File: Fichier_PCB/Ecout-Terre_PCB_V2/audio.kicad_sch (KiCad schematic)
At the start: 32 parts, among them J12 Conn_test_ampli, J14 AudioJack_Mono, U5 TL072, U6 LM386

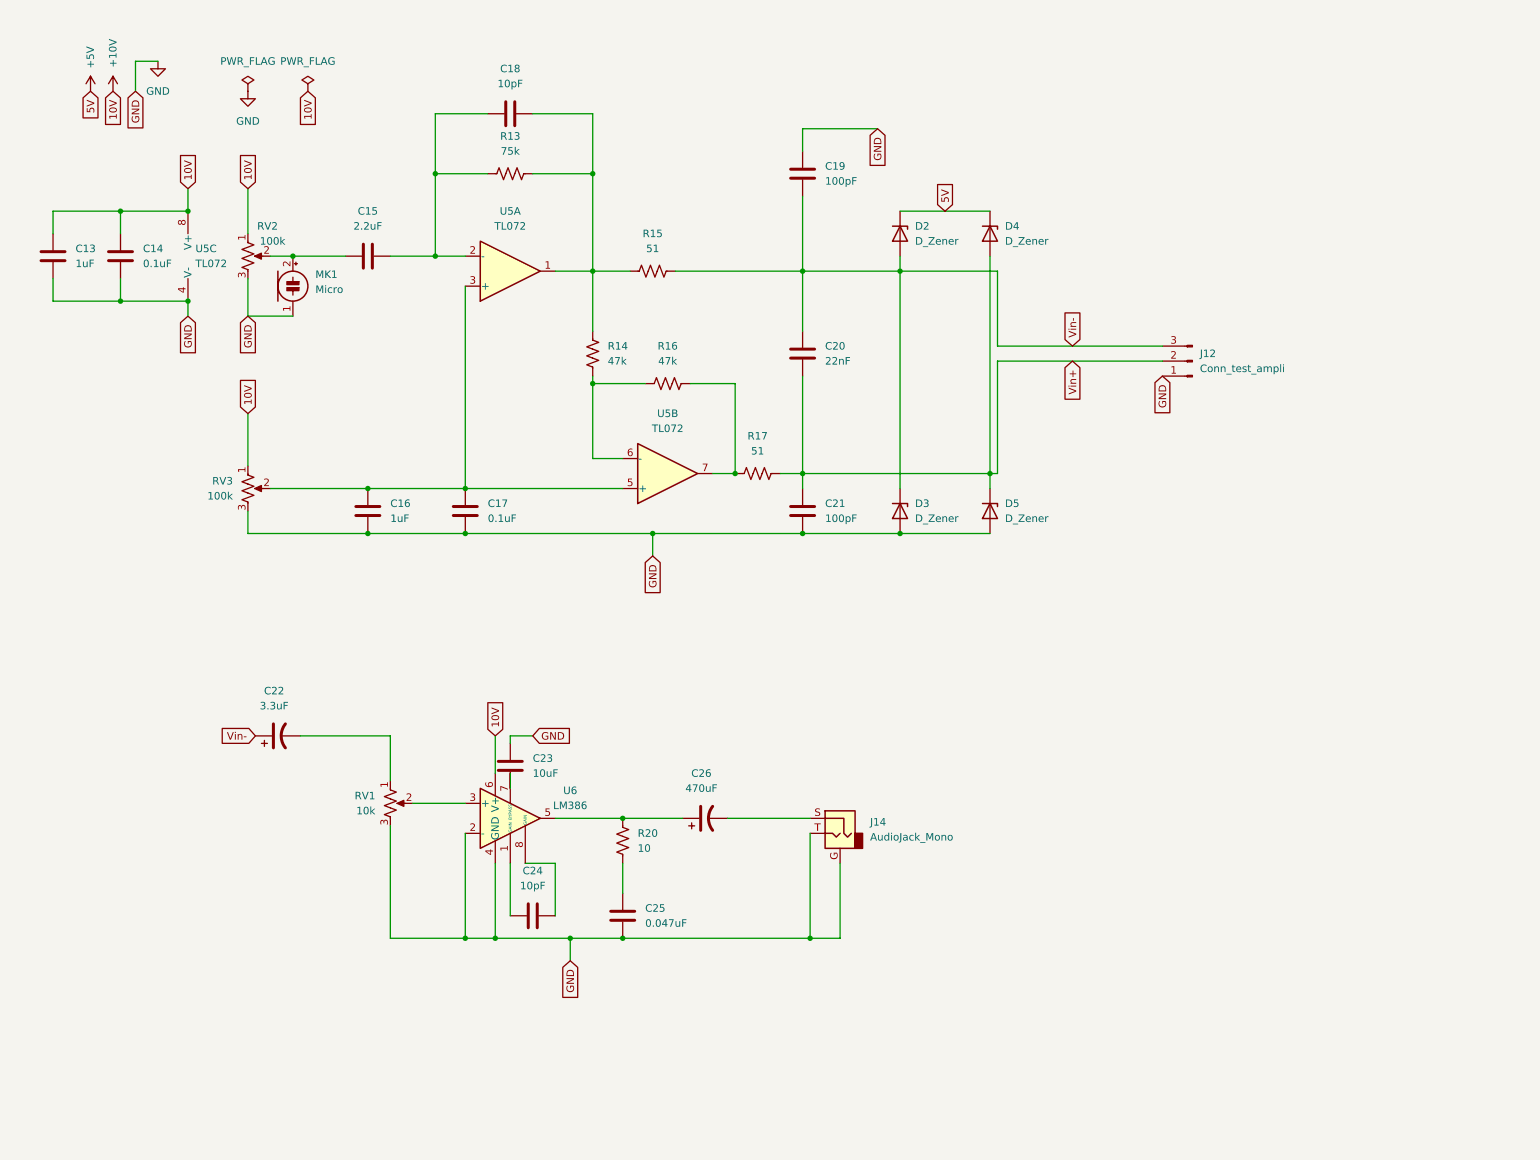
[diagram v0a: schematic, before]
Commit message: Trace pcb
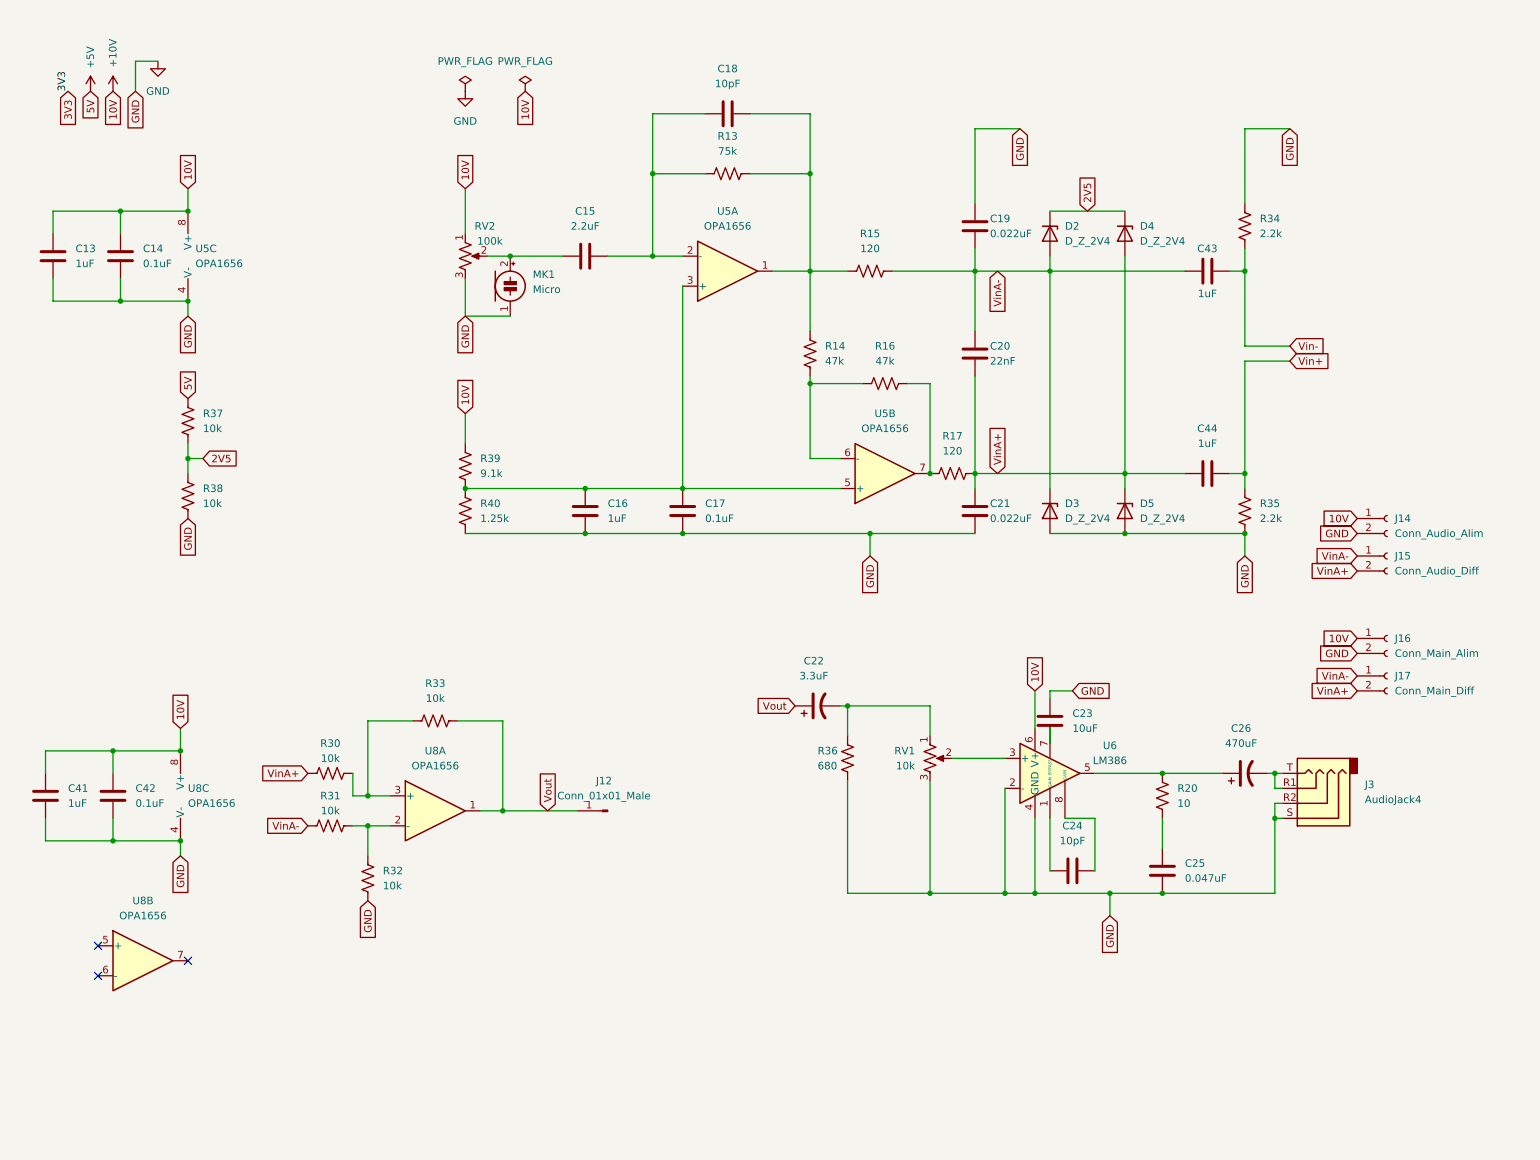
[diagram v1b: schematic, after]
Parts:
- removed J12: Conn_test_ampli, Connector_PinHeader_2.54mm:PinHeader_1x03_P2.54mm_Vertical, symbol Connector:Conn_01x03_Male
- removed J14: AudioJack_Mono, Audio:3_5mm_audioJack, symbol Connector:AudioJack2_Ground
- removed RV3: 100k, Potentiometer_THT:Potentiometer_Bourns_3296W_Vertical, symbol Device:R_Potentiometer_US
- added C41, C43, C44: 1uF, Capacitor_SMD:C_0805_2012Metric_Pad1.18x1.45mm_HandSolder, symbol Device:C
- added C42: 0.1uF, Capacitor_SMD:C_0805_2012Metric_Pad1.18x1.45mm_HandSolder, symbol Device:C
- added J12: Conn_01x01_Male, Connector_PinSocket_2.54mm:PinSocket_1x01_P2.54mm_Vertical, symbol Connector:Conn_01x01_Male
- added J14: Conn_Audio_Alim, Connector_Wire:SolderWire-0.75sqmm_1x02_P4.8mm_D1.25mm_OD2.3mm, symbol Connector:Conn_01x02_Female
- added J15: Conn_Audio_Diff, Connector_Wire:SolderWire-0.75sqmm_1x02_P4.8mm_D1.25mm_OD2.3mm, symbol Connector:Conn_01x02_Female
- added J16: Conn_Main_Alim, Connector_Wire:SolderWire-0.75sqmm_1x02_P4.8mm_D1.25mm_OD2.3mm, symbol Connector:Conn_01x02_Female
- added J17: Conn_Main_Diff, Connector_Wire:SolderWire-0.75sqmm_1x02_P4.8mm_D1.25mm_OD2.3mm, symbol Connector:Conn_01x02_Female
- added J3: AudioJack4, Connector_Audio:Jack_3.5mm_CUI_SJ-3524-SMT_Horizontal, symbol Connector:AudioJack4
- added R30, R31, R32, R33, R37, R38: 10k, Resistor_SMD:R_0805_2012Metric_Pad1.20x1.40mm_HandSolder, symbol Device:R_US
- added R34, R35: 2.2k, Resistor_SMD:R_0805_2012Metric_Pad1.20x1.40mm_HandSolder, symbol Device:R_US
- added R36: 680, Resistor_SMD:R_0805_2012Metric_Pad1.20x1.40mm_HandSolder, symbol Device:R_US
- added R39: 9.1k, Resistor_SMD:R_0805_2012Metric_Pad1.20x1.40mm_HandSolder, symbol Device:R_US
- added R40: 1.25k, Resistor_SMD:R_0805_2012Metric_Pad1.20x1.40mm_HandSolder, symbol Device:R_US
- added U8: OPA1656, Package_SO:SOIC-8_3.9x4.9mm_P1.27mm, symbol Amplifier_Operational:TL072
- C19, C21: value 100pF -> 0.022uF
- D2, D3, D4, D5: value D_Zener -> D_Z_2V4
- MK1: footprint TerminalBlock:TerminalBlock_bornier-2_P5.08mm -> Connector_Wire:SolderWire-0.1sqmm_1x02_P3.6mm_D0.4mm_OD1mm
- R15, R17: value 51 -> 120
- RV2: footprint Potentiometer_THT:Potentiometer_Bourns_3296W_Vertical -> Potentiometer_SMD:Potentiometer_Bourns_TC33X_Vertical
- U5: value TL072 -> OPA1656; footprint Custom_SOIC:SOIC-8_3.9_et_5.3mm -> Package_SO:SOIC-8_3.9x4.9mm_P1.27mm
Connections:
- net +10V: now also C41.2, C42.2, J14.1 (Pin_1), J16.1 (Pin_1), R39.1, U8.8 (V+)
- net +5V: now also R37.2; no longer D2.1 (K), D4.1 (K)
- net GND: now also C41.1, C42.1, J14.2 (Pin_2), J16.2 (Pin_2), J3.R2, J3.S, R32.1, R34.1, R35.2, R36.1, R38.1, R40.2, U8.4 (V-)
- net Vin+: now also C44.1, R35.1; no longer C20.1, C21.2, D4.2 (A), D5.1 (K), R17.2
- net Vin-: now also C43.1, R34.2; no longer C19.1, C20.2, C22.1, D2.2 (A), D3.1 (K), R15.2
- net at C16.2, C17.2, U5.3 (+)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: now also R39.2, R40.1
- net at C26.2: now also J3.R1, J3.T
- net at C22.2, RV1.1: now also R36.2
- new net: R31.2, R32.2, U8.2 (-)
- new net: R30.2, R33.1, U8.3 (+)
- new net 2V5: D2.1 (K), D4.1 (K), R37.1, R38.2
- new net VinA+: C20.1, C21.2, C44.2, D4.2 (A), D5.1 (K), J15.2 (Pin_2), J17.2 (Pin_2), R17.2, R30.1
- new net VinA-: C19.1, C20.2, C43.2, D2.2 (A), D3.1 (K), J15.1 (Pin_1), J17.1 (Pin_1), R15.2, R31.1
- new net Vout: C22.1, J12.1 (Pin_1), R33.2, U8.1
- no-connect marks 0 -> 3
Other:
- moved on the sheet: C15, C16, C17, C18, C19, C20, C21, C22, C23, C24, C25, C26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

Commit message: Clarification du schéma pcb
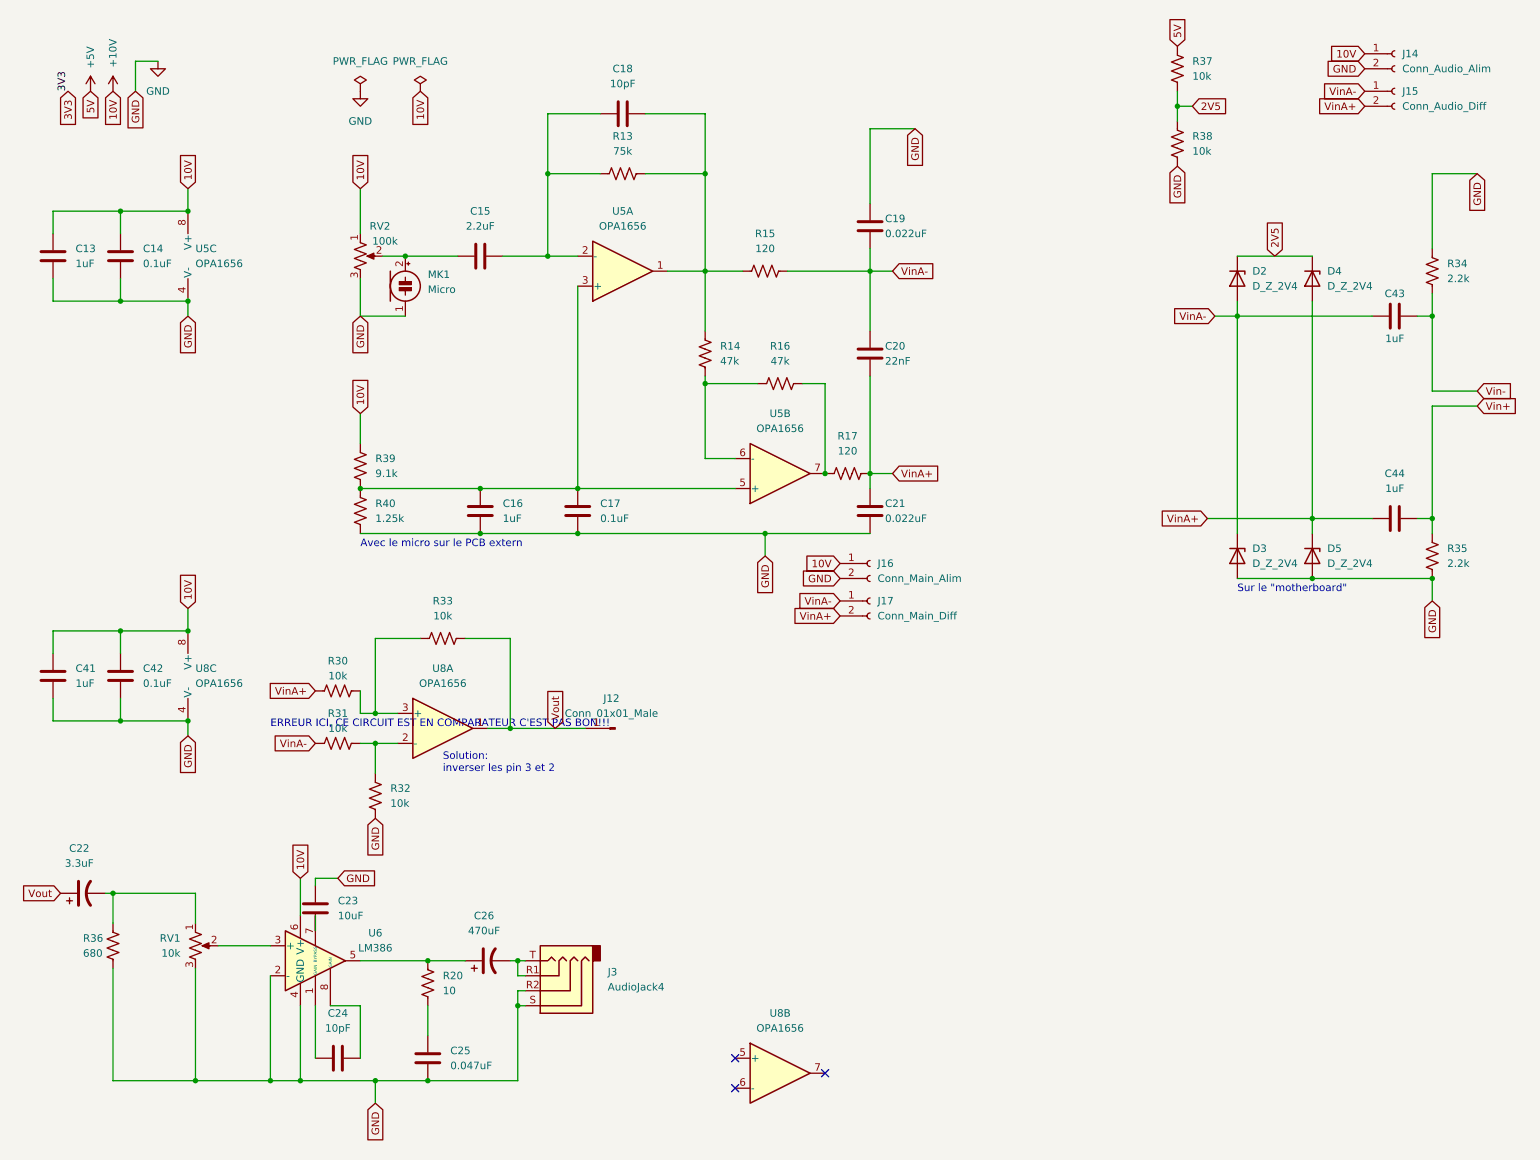
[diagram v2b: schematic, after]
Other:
- note added: "Avec le micro sur le PCB extern"
- note added: "ERREUR ICI, CE CIRCUIT EST EN COMPARATEUR C'EST PAS BON!!!"
- note added: "Solution: inverser les pin 3 et 2"
- note added: "Sur le "motherboard""
- moved on the sheet: C15, C16, C17, C18, C19, C20, C21, C22, C23, C24, C25, C26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
